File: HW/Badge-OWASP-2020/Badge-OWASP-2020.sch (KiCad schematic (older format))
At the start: 25 parts, among them J1 Screw_Terminal_01x04, J2 USB_B, J3 Conn_02x03_Odd_Even, Q1 MMBT3904, Q2 MMBT3904, SW1 RST, SW2 BOOT, U1 AP111733, U2 ESP32-WROOM-32, U3 CH340C

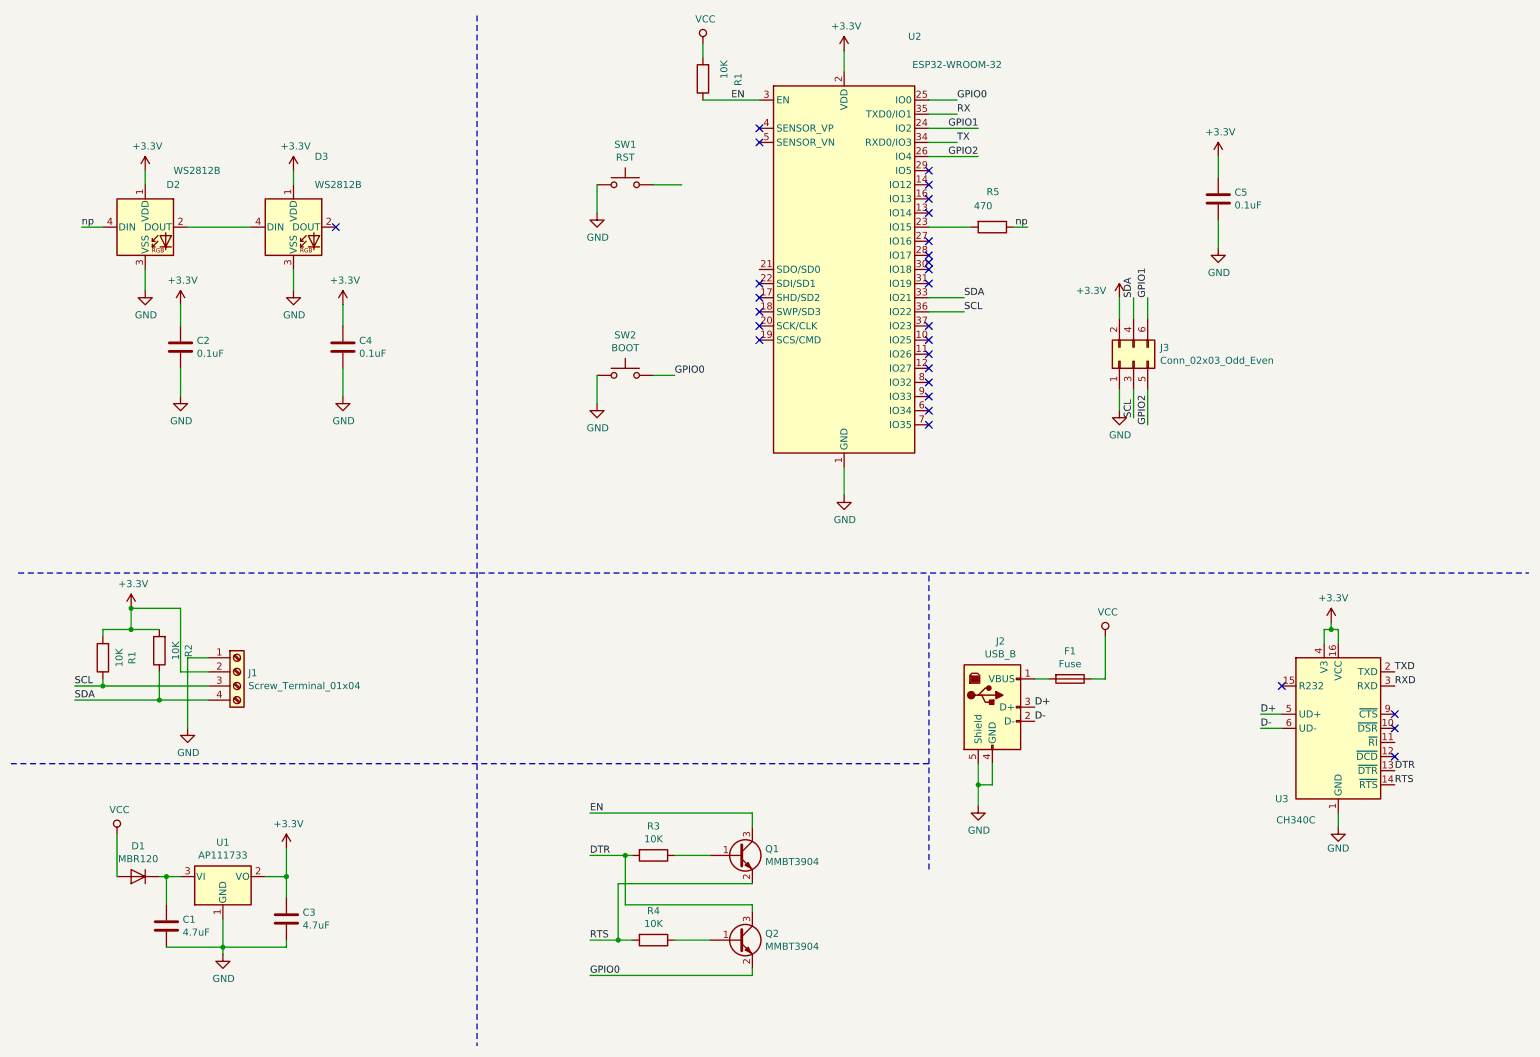
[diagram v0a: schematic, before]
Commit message: add labels and fix voltage
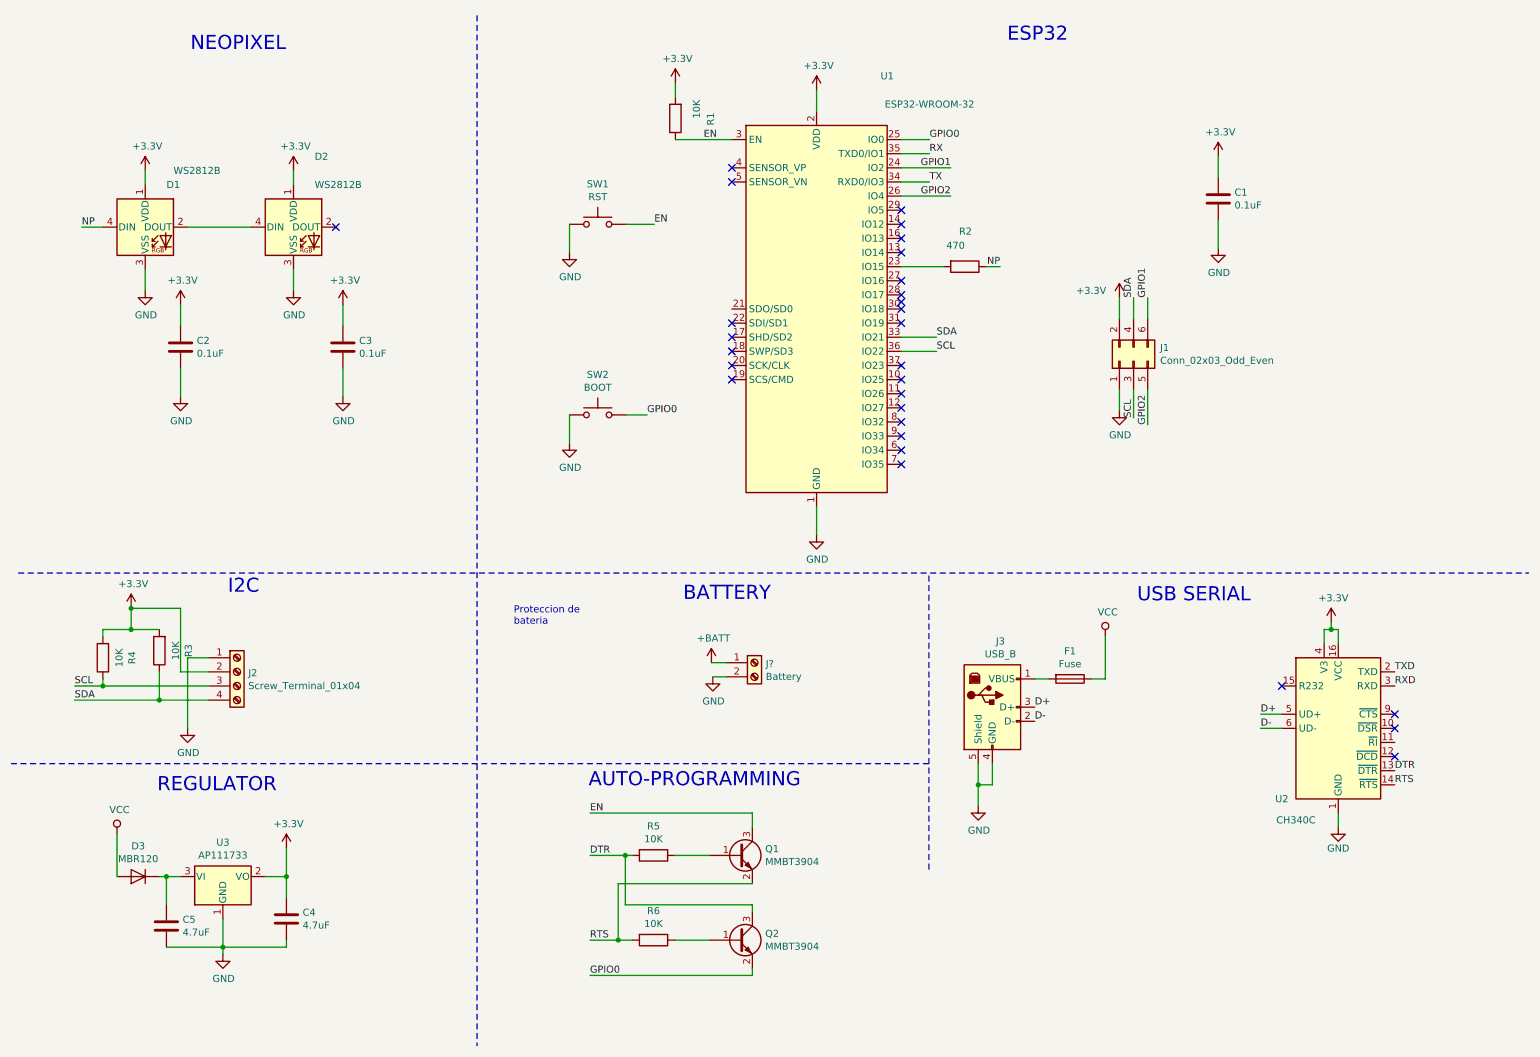
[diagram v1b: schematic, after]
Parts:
- added J?: Battery, symbol Connector:Screw_Terminal_01x02
- renumbered C5 to C1, C4 to C3, C3 to C4, C1 to C5, D2 to D1, D3 to D2, D1 to D3, J3 to J1, J1 to J2, J2 to J3, R5 to R2, R2 to R3, R1 to R4, R3 to R5, R4 to R6, U2 to U1, U3 to U2, U1 to U3
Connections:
- net +3V3: now also R1.2
- net EN: now also SW1.2
- net GND: now also J?.2 (Pin_2)
- net VCC: no longer R1.2
- net np renamed NP
- new net +BATT: J?.1 (Pin_1)
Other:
- note added: "AUTO-PROGRAMMING"
- note added: "BATTERY"
- note added: "ESP32"
- note added: "I2C"
- note added: "NEOPIXEL"
- note added: "Proteccion de \nbateria"
- note added: "REGULATOR"
- note added: "USB SERIAL"
- moved on the sheet: R1, R2, SW1, SW2, U1

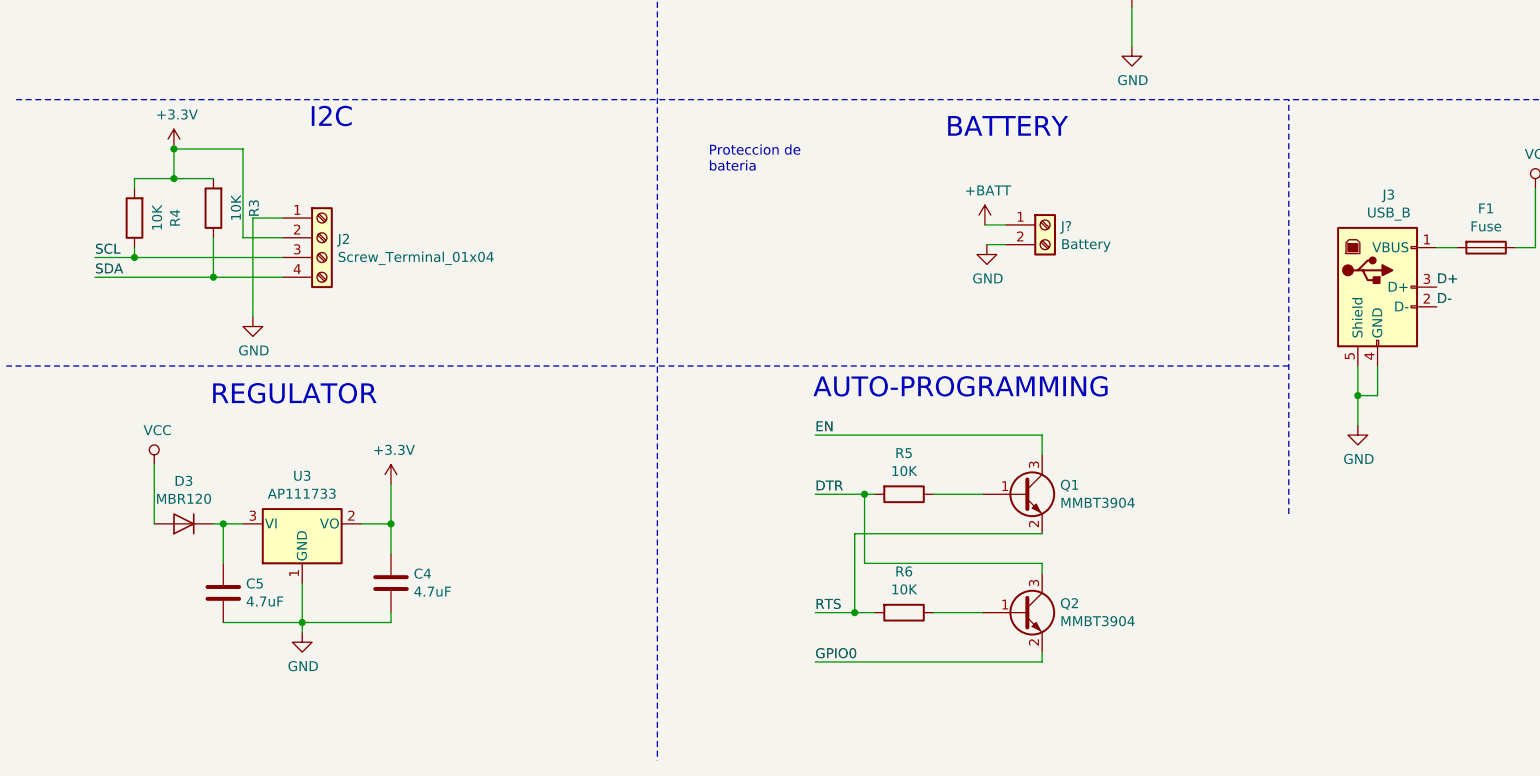
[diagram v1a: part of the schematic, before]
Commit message: add battery and protection
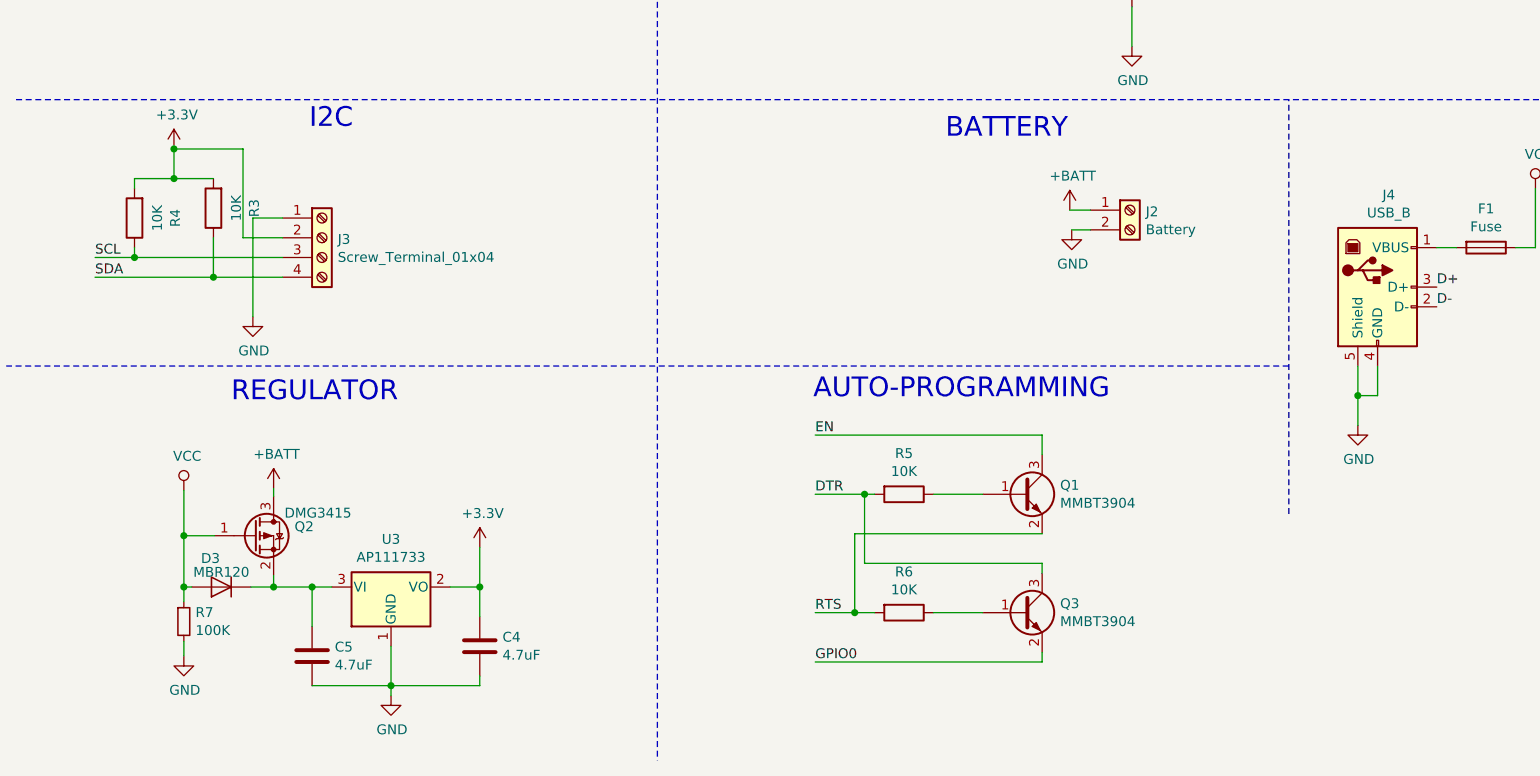
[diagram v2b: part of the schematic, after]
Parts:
- added Q2: DMG3415, Package_TO_SOT_SMD:SOT-23, symbol Transistor_FET:DMG2301L
- added R7: 100K, Resistor_SMD:R_0805_2012Metric_Pad1.15x1.40mm_HandSolder, symbol Device:R_Small
- J2: renamed from J?; footprint (none) -> Connector_PinHeader_2.54mm:PinHeader_1x02_P2.54mm_Vertical
- renumbered J2 to J3, J3 to J4, Q2 to Q3
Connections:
- net +BATT: now also Q2.3 (D)
- net GND: now also R7.2
- net VCC: now also Q2.1 (G), R7.1
- net at C5.1, D3.1 (K), U3.3 (VI): now also Q2.2 (S)
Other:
- note removed: "Proteccion de \nbateria"
- moved on the sheet: C4, C5, D3, J2, U3

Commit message: Update labels
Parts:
- J1: value Conn_02x03_Odd_Even -> Shitty Add-Ons
- J3: value Screw_Terminal_01x04 -> I2C
- Q2: value DMG3415 -> DMG3415U-7
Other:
- moved on the sheet: J2
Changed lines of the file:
@@
 P 2050 5150
 F 0 "J3" H 2130 5142 50  0000 L CNN
-F 1 "Screw_Terminal_01x04" H 2130 5051 50  0000 L CNN
+F 1 "I2C" H 2130 5051 50  0000 L CNN
 F 2 "Connector_PinHeader_2.54mm:PinHeader_1x04_P2.54mm_Vertical" H 2050 5150 50  0001 C CNN
 F 3 "~" H 2050 5150 50  0001 C CNN
@@
 P 8400 2950
 F 0 "J1" V 8496 2762 50  0000 R CNN
-F 1 "Conn_02x03_Odd_Even" V 8405 2762 50  0000 R CNN
+F 1 "Shitty Add-Ons" V 8405 2762 50  0000 R CNN
 F 2 "Connector_PinHeader_2.54mm:PinHeader_2x03_P2.54mm_Vertical" H 8400 2950 50  0001 C CNN
 F 3 "~" H 8400 2950 50  0001 C CNN
@@
 Text Notes 1985 4605 0    100  ~ 0
 I2C
-Text Notes 5210 4655 0    100  ~ 0
+Text Notes 4960 4640 0    100  ~ 0
 BATTERY
 $Comp
 L Connector:Screw_Terminal_01x02 J2
 U 1 1 5DFEA819
-P 6145 5010
-F 0 "J2" H 6225 5002 50  0000 L CNN
-F 1 "Battery" H 6225 4911 50  0000 L CNN
-F 2 "Connector_PinHeader_2.54mm:PinHeader_1x02_P2.54mm_Vertical" H 6145 5010 50  0001 C CNN
-F 3 "~" H 6145 5010 50  0001 C CNN
-	1    6145 5010
-	1    0    0    -1
-$EndComp
-Wire Wire Line
-	5945 5010 5840 5010
-Wire Wire Line
-	5945 5110 5850 5110
+P 5505 5105
+F 0 "J2" H 5585 5097 50  0000 L CNN
+F 1 "Battery" H 5585 5006 50  0000 L CNN
+F 2 "Connector_PinHeader_2.54mm:PinHeader_1x02_P2.54mm_Vertical" H 5505 5105 50  0001 C CNN
+F 3 "~" H 5505 5105 50  0001 C CNN
+	1    5505 5105
+	1    0    0    -1
+$EndComp
+Wire Wire Line
+	5305 5105 5200 5105
+Wire Wire Line
+	5305 5205 5210 5205
 $Comp
 L power:GND #PWR022
 U 1 1 5DFF084A
-P 5850 5110
-F 0 "#PWR022" H 5850 4860 50  0001 C CNN
-F 1 "GND" H 5855 4937 50  0000 C CNN
-F 2 "" H 5850 5110 50  0001 C CNN
-F 3 "" H 5850 5110 50  0001 C CNN
-	1    5850 5110
+P 5210 5205
+F 0 "#PWR022" H 5210 4955 50  0001 C CNN
+F 1 "GND" H 5215 5032 50  0000 C CNN
+F 2 "" H 5210 5205 50  0001 C CNN
+F 3 "" H 5210 5205 50  0001 C CNN
+	1    5210 5205
 	1    0    0    -1
 $EndComp
@@
 L power:+BATT #PWR021
 U 1 1 5DFF1DD9
-P 5840 5010
-F 0 "#PWR021" H 5840 4860 50  0001 C CNN
-F 1 "+BATT" H 5855 5183 50  0000 C CNN
-F 2 "" H 5840 5010 50  0001 C CNN
-F 3 "" H 5840 5010 50  0001 C CNN
-	1    5840 5010
+P 5200 5105
+F 0 "#PWR021" H 5200 4955 50  0001 C CNN
+F 1 "+BATT" H 5215 5278 50  0000 C CNN
+F 2 "" H 5200 5105 50  0001 C CNN
+F 3 "" H 5200 5105 50  0001 C CNN
+	1    5200 5105
 	1    0    0    -1
 $EndComp
@@
 P 1705 6660
 F 0 "Q2" H 1911 6706 50  0000 L CNN
-F 1 "DMG3415" H 1860 6775 50  0000 L CNN
+F 1 "DMG3415U-7" H 1860 6775 50  0000 L CNN
 F 2 "Package_TO_SOT_SMD:SOT-23" H 1905 6585 50  0001 L CIN
 F 3 "https://www.diodes.com/assets/Datasheets/DMG2301L.pdf" H 1705 6660 50  0001 L CNN
